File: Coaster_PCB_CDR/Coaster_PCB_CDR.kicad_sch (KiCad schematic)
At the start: 29 parts, among them J1 Vin, J10 GPIO_27-28, J11 5v, J2 HC-05, J3 3v3, J4 5v, J5 qwiic, J6 GPIO_0-1, J7 qwiic, J8 GPIO_14-15, J9 3v3, SW1 sigma, SW2 alpha, U1 PicoW, U2 LM1084-5.0, U3 LM2937xT

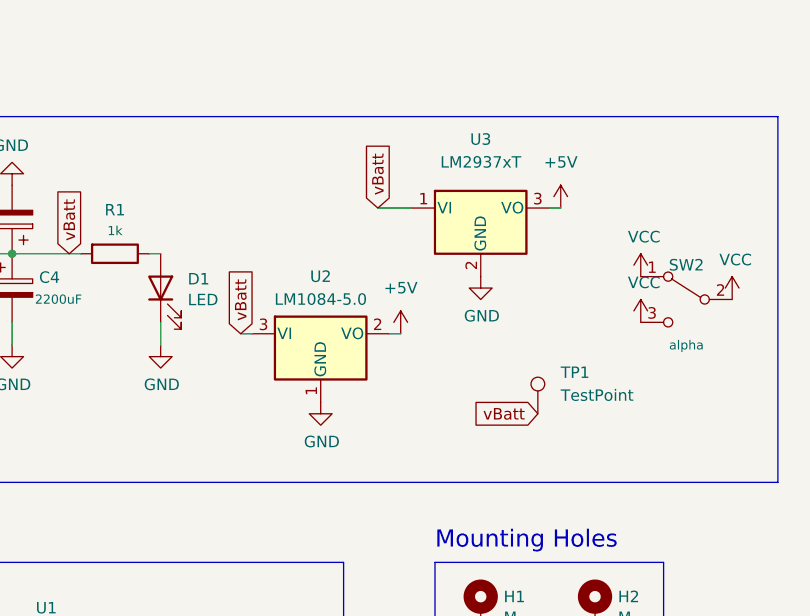
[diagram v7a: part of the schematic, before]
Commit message: added couple ceramics
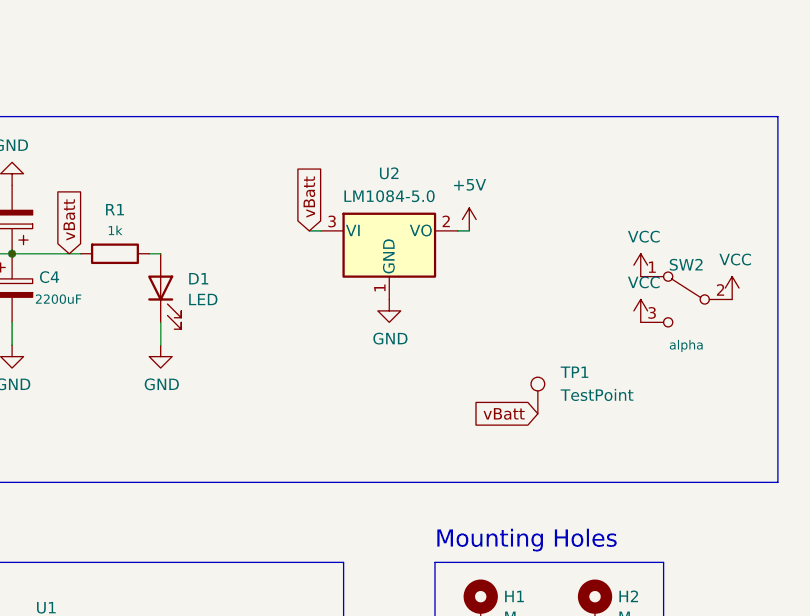
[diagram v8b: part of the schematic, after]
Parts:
- removed U3: LM2937xT, Package_TO_SOT_THT:TO-220-3_Vertical, symbol Regulator_Linear:LM2937xT
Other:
- moved on the sheet: U2
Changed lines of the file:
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@@
-    (stroke (width 0) (type default) (color 0 0 0 0))
-  )
-  (wire (pts (xy 120.65 40.64) (xy 124.46 40.64))
-    (stroke (width 0) (type default) (color 0 0 0 0))
-  )
-  (wire (pts (xy 140.97 40.64) (xy 139.7 40.64))
     (stroke (width 0) (type default) (color 0 0 0 0))
   )
@@
     (stroke (width 0) (type default) (color 0 0 0 0))
   )
-  (wire (pts (xy 105.41 54.61) (xy 106.68 54.61))
+  (wire (pts (xy 113.03 43.18) (xy 114.3 43.18))
     (stroke (width 0) (type default) (color 0 0 0 0))
   )
@@
     (stroke (width 0) (type default) (color 0 0 0 0))
   )
-  (wire (pts (xy 123.19 54.61) (xy 121.92 54.61))
+  (wire (pts (xy 130.81 43.18) (xy 129.54 43.18))
     (stroke (width 0) (type default) (color 0 0 0 0))
   )
@@
     )
   )
-  (global_label "vBatt" (shape input) (at 120.65 40.64 90) (fields_autoplaced)
-    (effects (font (size 1.27 1.27)) (justify left))
-    (property "Intersheet References" "${INTERSHEET_REFS}" (id 0) (at 120.5706 33.3888 90)
-      (effects (font (size 1.27 1.27)) (justify left) hide)
-    )
-  )
   (global_label "GPIO1" (shape input) (at 57.15 95.25 180) (fields_autoplaced)
     (effects (font (size 1.27 1.27)) (justify right))
@@
     )
   )
-  (global_label "vBatt" (shape input) (at 105.41 54.61 90) (fields_autoplaced)
-    (effects (font (size 1.27 1.27)) (justify left))
-    (property "Intersheet References" "${INTERSHEET_REFS}" (id 0) (at 105.3306 47.3588 90)
+  (global_label "vBatt" (shape input) (at 113.03 43.18 90) (fields_autoplaced)
+    (effects (font (size 1.27 1.27)) (justify left))
+    (property "Intersheet References" "${INTERSHEET_REFS}" (id 0) (at 112.9506 35.9288 90)
       (effects (font (size 1.27 1.27)) (justify left) hide)
     )
@@
     (pin "1")
   )
-  (symbol (lib_id "power:GND") (at 114.3 62.23 0) (unit 1)
-    (in_bom yes) (on_board yes)
-    (property "Reference" "#PWR018" (id 0) (at 114.3 68.58 0)
-      (effects (font (size 1.27 1.27)) hide)
-    )
-    (property "Value" "GND" (id 1) (at 114.427 66.6242 0))
-    (property "Footprint" "" (id 2) (at 114.3 62.23 0)
-      (effects (font (size 1.27 1.27)) hide)
-    )
-    (property "Datasheet" "" (id 3) (at 114.3 62.23 0)
+  (symbol (lib_id "power:GND") (at 121.92 50.8 0) (unit 1)
+    (in_bom yes) (on_board yes)
+    (property "Reference" "#PWR018" (id 0) (at 121.92 57.15 0)
+      (effects (font (size 1.27 1.27)) hide)
+    )
+    (property "Value" "GND" (id 1) (at 122.047 55.1942 0))
+    (property "Footprint" "" (id 2) (at 121.92 50.8 0)
+      (effects (font (size 1.27 1.27)) hide)
+    )
+    (property "Datasheet" "" (id 3) (at 121.92 50.8 0)
       (effects (font (size 1.27 1.27)) hide)
     )
@@
     (pin "2")
   )
-  (symbol (lib_id "power:GND") (at 132.08 48.26 0) (unit 1)
-    (in_bom yes) (on_board yes)
-    (property "Reference" "#PWR021" (id 0) (at 132.08 54.61 0)
-      (effects (font (size 1.27 1.27)) hide)
-    )
-    (property "Value" "GND" (id 1) (at 132.207 52.6542 0))
-    (property "Footprint" "" (id 2) (at 132.08 48.26 0)
-      (effects (font (size 1.27 1.27)) hide)
-    )
-    (property "Datasheet" "" (id 3) (at 132.08 48.26 0)
-      (effects (font (size 1.27 1.27)) hide)
-    )
-    (pin "1")
-  )
   (symbol (lib_id "power:+5V") (at 142.24 142.24 0) (unit 1)
     (in_bom yes) (on_board yes) (fields_autoplaced)
@@
     (pin "1")
   )
-  (symbol (lib_id "Regulator_Linear:LM2937xT") (at 132.08 40.64 0) (unit 1)
-    (in_bom yes) (on_board yes) (fields_autoplaced)
-    (property "Reference" "U3" (id 0) (at 132.08 33.02 0))
-    (property "Value" "LM2937xT" (id 1) (at 132.08 35.56 0))
-    (property "Footprint" "Package_TO_SOT_THT:TO-220-3_Vertical" (id 2) (at 132.08 34.925 0)
-      (effects (font (size 1.27 1.27) italic) hide)
-    )
-    (property "Datasheet" "http://www.ti.com/lit/ds/symlink/lm2937.pdf" (id 3) (at 132.08 41.91 0)
-      (effects (font (size 1.27 1.27)) hide)
-    )
-    (pin "1")
-    (pin "2")
-    (pin "3")
-  )
   (symbol (lib_id "power:VCC") (at 149.86 53.34 0) (unit 1)
     (in_bom yes) (on_board yes)
@@
     (pin "1")
   )
-  (symbol (lib_id "power:+5V") (at 123.19 54.61 0) (unit 1)
+  (symbol (lib_id "power:+5V") (at 130.81 43.18 0) (unit 1)
     (in_bom yes) (on_board yes) (fields_autoplaced)
-    (property "Reference" "#PWR019" (id 0) (at 123.19 58.42 0)
-      (effects (font (size 1.27 1.27)) hide)
-    )
-    (property "Value" "+5V" (id 1) (at 123.19 49.53 0))
-    (property "Footprint" "" (id 2) (at 123.19 54.61 0)
-      (effects (font (size 1.27 1.27)) hide)
-    )
-    (property "Datasheet" "" (id 3) (at 123.19 54.61 0)
+    (property "Reference" "#PWR019" (id 0) (at 130.81 46.99 0)
+      (effects (font (size 1.27 1.27)) hide)
+    )
+    (property "Value" "+5V" (id 1) (at 130.81 38.1 0))
+    (property "Footprint" "" (id 2) (at 130.81 43.18 0)
+      (effects (font (size 1.27 1.27)) hide)
+    )
+    (property "Datasheet" "" (id 3) (at 130.81 43.18 0)
       (effects (font (size 1.27 1.27)) hide)
     )
@@
     (pin "5")
     (pin "6")
-  )
-  (symbol (lib_id "power:+5V") (at 140.97 40.64 0) (unit 1)
-    (in_bom yes) (on_board yes) (fields_autoplaced)
-    (property "Reference" "#PWR025" (id 0) (at 140.97 44.45 0)
-      (effects (font (size 1.27 1.27)) hide)
-    )
-    (property "Value" "+5V" (id 1) (at 140.97 35.56 0))
-    (property "Footprint" "" (id 2) (at 140.97 40.64 0)
-      (effects (font (size 1.27 1.27)) hide)
-    )
-    (property "Datasheet" "" (id 3) (at 140.97 40.64 0)
-      (effects (font (size 1.27 1.27)) hide)
-    )
-    (pin "1")
   )
   (symbol (lib_id "power:GND") (at 80.01 38.1 180) (unit 1)
@@
     (pin "9")
   )
-  (symbol (lib_id "Regulator_Linear:LM1084-5.0") (at 114.3 54.61 0) (unit 1)
-    (in_bom yes) (on_board yes)
-    (property "Reference" "U2" (id 0) (at 114.3 48.26 0))
-    (property "Value" "LM1084-5.0" (id 1) (at 114.3 50.8 0))
-    (property "Footprint" "Package_TO_SOT_THT:TO-220-3_Vertical" (id 2) (at 114.3 48.26 0)
+  (symbol (lib_id "Regulator_Linear:LM1084-5.0") (at 121.92 43.18 0) (unit 1)
+    (in_bom yes) (on_board yes)
+    (property "Reference" "U2" (id 0) (at 121.92 36.83 0))
+    (property "Value" "LM1084-5.0" (id 1) (at 121.92 39.37 0))
+    (property "Footprint" "Package_TO_SOT_THT:TO-220-3_Vertical" (id 2) (at 121.92 36.83 0)
       (effects (font (size 1.27 1.27) italic) hide)
     )
-    (property "Datasheet" "http://www.ti.com/lit/ds/symlink/lm1084.pdf" (id 3) (at 114.3 54.61 0)
+    (property "Datasheet" "http://www.ti.com/lit/ds/symlink/lm1084.pdf" (id 3) (at 121.92 43.18 0)
       (effects (font (size 1.27 1.27)) hide)
     )
@@
       (reference "#PWR020") (unit 1) (value "+3.3V") (footprint "")
     )
-    (path "/38fa52b0-506c-432a-b23e-d0fb47dbb888"
-      (reference "#PWR021") (unit 1) (value "GND") (footprint "")
-    )
     (path "/5a12c58c-d291-4965-9984-e414a0333d21"
       (reference "#PWR022") (unit 1) (value "GND") (footprint "")
@@
       (reference "#PWR024") (unit 1) (value "+5V") (footprint "")
     )
-    (path "/ac46a6b9-e4d7-45f4-afa0-0a74ae97fc44"
-      (reference "#PWR025") (unit 1) (value "+5V") (footprint "")
-    )
     (path "/3e5d933d-3c40-414f-8f8a-7b9e4e525f03"
       (reference "#PWR026") (unit 1) (value "+5V") (footprint "")
@@
       (reference "U2") (unit 1) (value "LM1084-5.0") (footprint "Package_TO_SOT_THT:TO-220-3_Vertical")
     )
-    (path "/9a1e93dd-bcd8-4f4f-bb33-c231142f3f81"
-      (reference "U3") (unit 1) (value "LM2937xT") (footprint "Package_TO_SOT_THT:TO-220-3_Vertical")
-    )
-  )
+  )
